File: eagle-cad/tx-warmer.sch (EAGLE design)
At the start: 22 parts

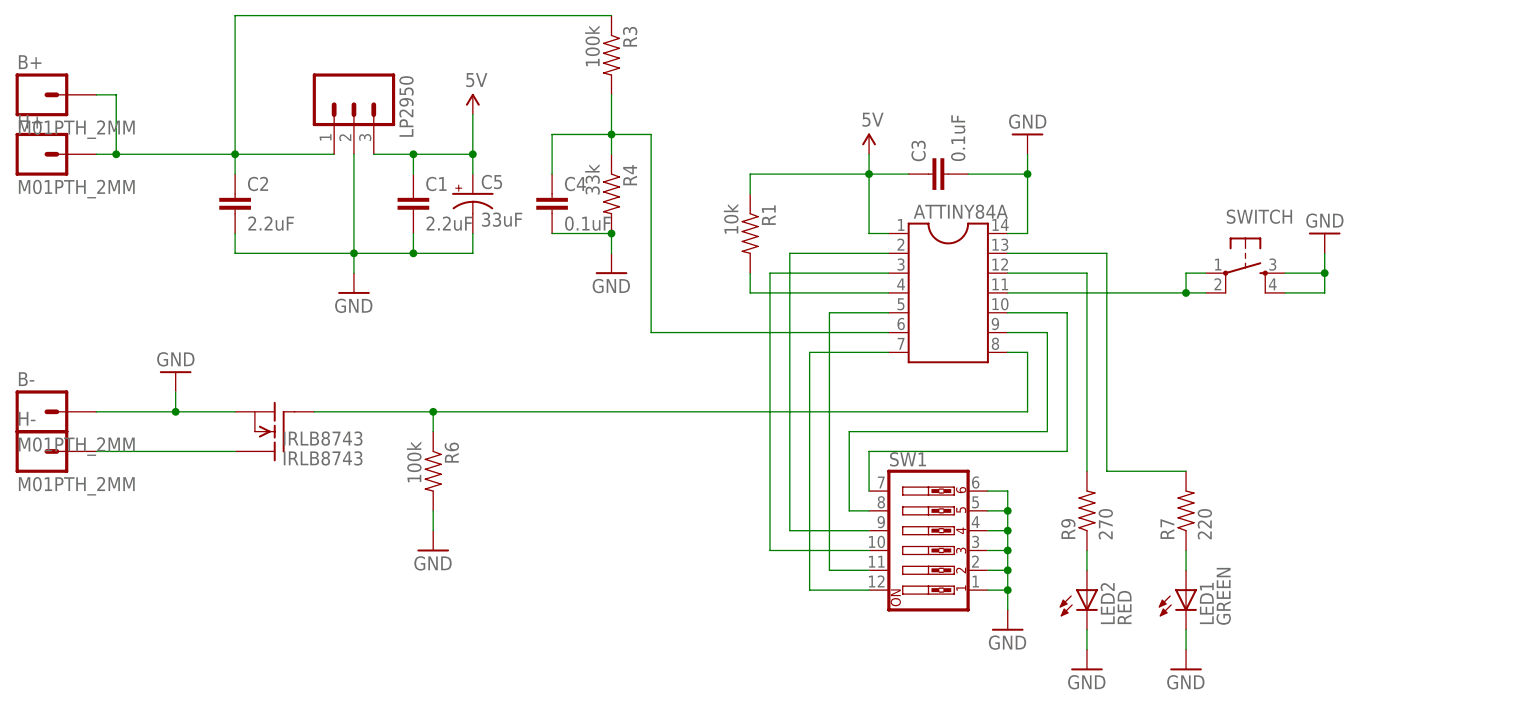
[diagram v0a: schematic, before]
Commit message: Removed DIP:s, added two sensor ports, bat-pins and prog-interface
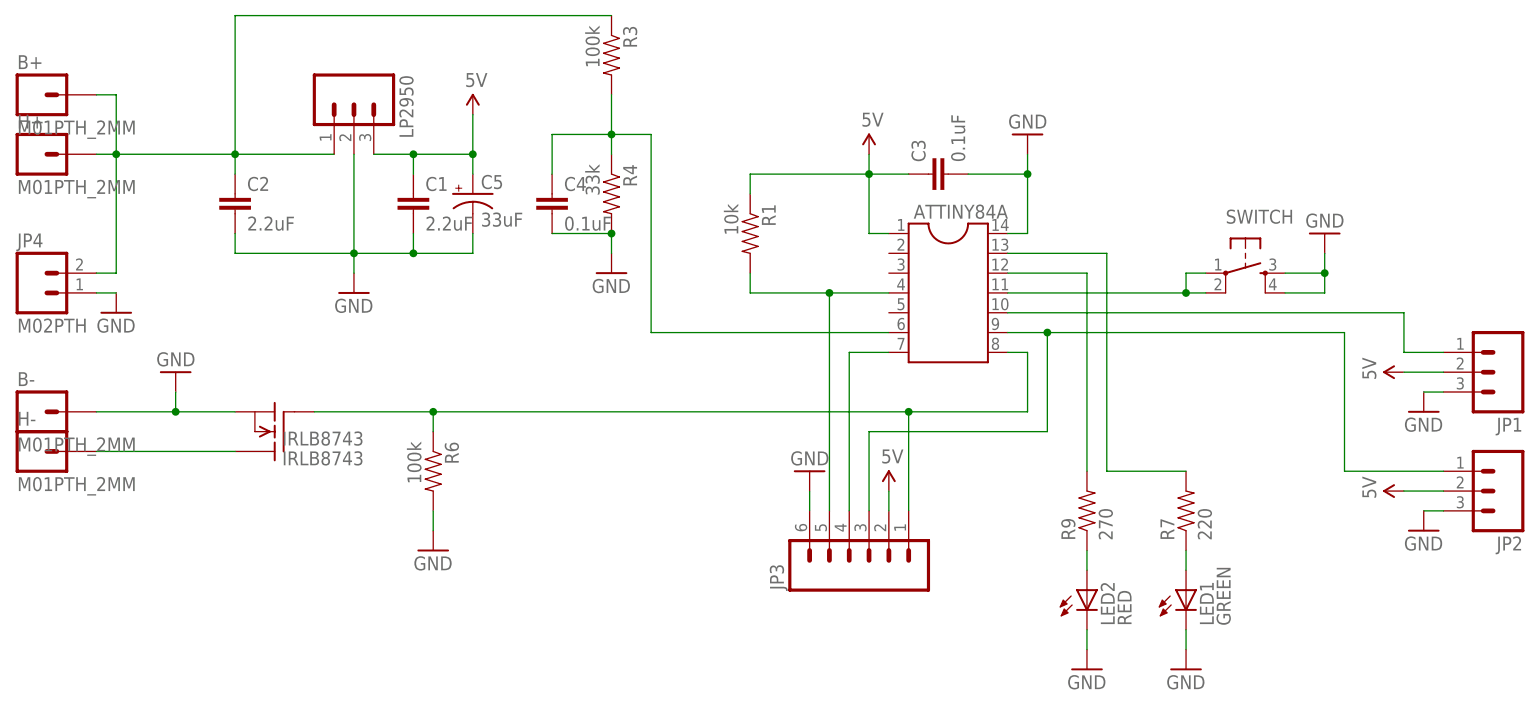
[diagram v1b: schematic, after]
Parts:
- removed SW1: (no value), special:SW_DIP-6
- added JP1, JP2: (no value), SparkFun-Connectors:M03PTH
- added JP3: (no value), SparkFun-Connectors:M06SIP
- added JP4: M02PTH, SparkFun-Connectors:M02PTH
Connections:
- removed net N$20: ATTINY84A.10, SW1.7
- removed net N$21: ATTINY84A.3, SW1.10
- removed net N$5: ATTINY84A.9, SW1.8
- net 5V: now also JP1.2, JP2.2, JP3.2
- net GND: now also JP1.3, JP2.3, JP3.6, JP4.1; no longer SW1.1, SW1.2, SW1.3, SW1.4, SW1.5, SW1.6
- net N$1: now also ATTINY84A.9, JP2.1, JP3.3; no longer ATTINY84A.7, SW1.12
- net N$11: now also JP3.5
- net N$2: now also ATTINY84A.7, JP3.4; no longer ATTINY84A.5, SW1.11
- net N$3: now also ATTINY84A.10, JP1.1; no longer ATTINY84A.2, SW1.9
- net N$4: now also JP4.2
- net N$6: now also JP3.1

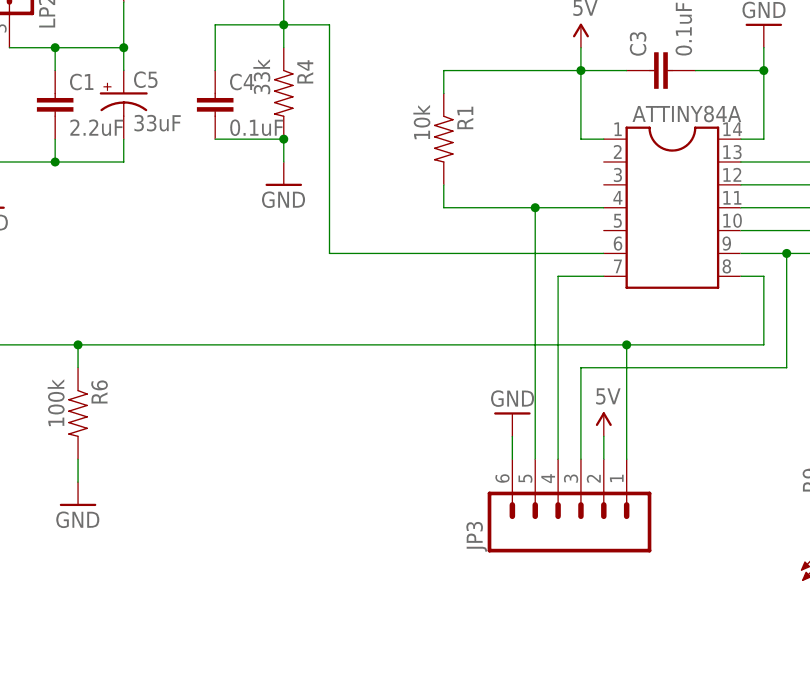
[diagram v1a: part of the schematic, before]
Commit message: Added SMD-jumpers to empty MC-pins
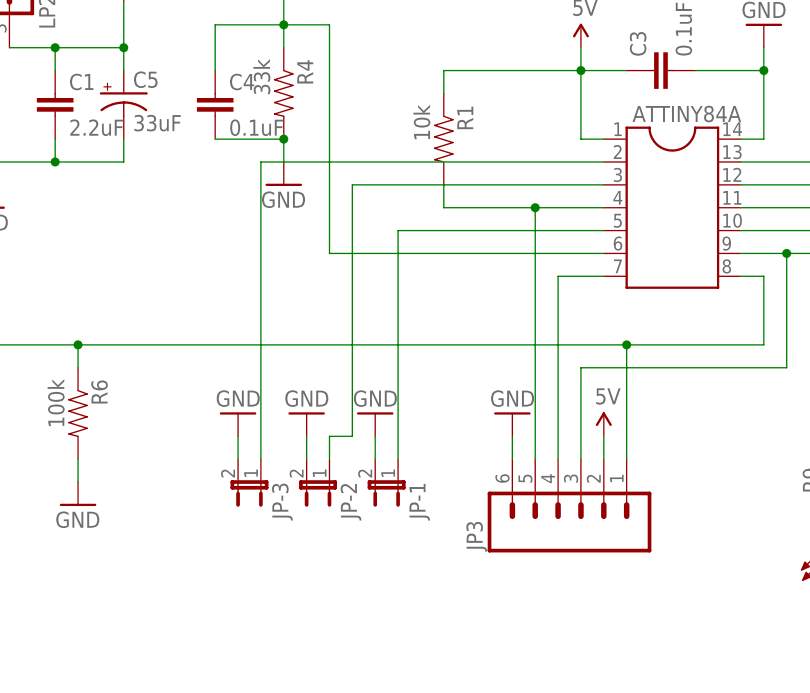
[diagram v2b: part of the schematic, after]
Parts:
- added JP-1, JP-2, JP-3: (no value), SparkFun-Passives:JUMPER-2SMD-NO
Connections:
- new net N$20: ATTINY84A.3, JP-2.1
- new net N$21: ATTINY84A.2, JP-3.1
- new net N$5: ATTINY84A.5, JP-1.1
- net GND: now also JP-1.2, JP-2.2, JP-3.2
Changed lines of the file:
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@@
 <part name="JP4" library="SparkFun-Connectors" deviceset="M02" device="PTH"/>
 <part name="GND12" library="SparkFun-Aesthetics" deviceset="GND" device=""/>
+<part name="JP-1" library="SparkFun-Passives" deviceset="JUMPER-2" device="SMD-NO"/>
+<part name="JP-2" library="SparkFun-Passives" deviceset="JUMPER-2" device="SMD-NO"/>
+<part name="JP-3" library="SparkFun-Passives" deviceset="JUMPER-2" device="SMD-NO"/>
+<part name="GND13" library="SparkFun-Aesthetics" deviceset="GND" device=""/>
+<part name="GND14" library="SparkFun-Aesthetics" deviceset="GND" device=""/>
+<part name="GND15" library="SparkFun-Aesthetics" deviceset="GND" device=""/>
 </parts>
 <sheets>
@@
 <instance part="JP4" gate="G$1" x="-5.08" y="53.34"/>
 <instance part="GND12" gate="1" x="5.08" y="50.8"/>
+<instance part="JP-1" gate="A" x="81.28" y="22.86" rot="R180"/>
+<instance part="JP-2" gate="A" x="73.66" y="22.86" rot="R180"/>
+<instance part="JP-3" gate="A" x="66.04" y="22.86" rot="R180"/>
+<instance part="GND13" gate="1" x="78.74" y="30.48" rot="R180"/>
+<instance part="GND14" gate="1" x="71.12" y="30.48" rot="R180"/>
+<instance part="GND15" gate="1" x="63.5" y="30.48" rot="R180"/>
 </instances>
 <busses>
@@
 <wire x1="2.54" y1="53.34" x2="5.08" y2="53.34" width="0.1524" layer="91"/>
 </segment>
+<segment>
+<pinref part="GND15" gate="1" pin="GND"/>
+<pinref part="JP-3" gate="A" pin="2"/>
+<wire x1="63.5" y1="27.94" x2="63.5" y2="25.4" width="0.1524" layer="91"/>
+</segment>
+<segment>
+<pinref part="GND14" gate="1" pin="GND"/>
+<pinref part="JP-2" gate="A" pin="2"/>
+<wire x1="71.12" y1="27.94" x2="71.12" y2="25.4" width="0.1524" layer="91"/>
+</segment>
+<segment>
+<pinref part="GND13" gate="1" pin="GND"/>
+<pinref part="JP-1" gate="A" pin="2"/>
+<wire x1="78.74" y1="27.94" x2="78.74" y2="25.4" width="0.1524" layer="91"/>
+</segment>
 </net>
 <net name="5V" class="0">
@@
 </segment>
 </net>
+<net name="N$5" class="0">
+<segment>
+<pinref part="ATTINY84A" gate="G$1" pin="5"/>
+<pinref part="JP-1" gate="A" pin="1"/>
+<wire x1="104.14" y1="50.8" x2="81.28" y2="50.8" width="0.1524" layer="91"/>
+<wire x1="81.28" y1="50.8" x2="81.28" y2="25.4" width="0.1524" layer="91"/>
+</segment>
+</net>
+<net name="N$20" class="0">
+<segment>
+<pinref part="ATTINY84A" gate="G$1" pin="3"/>
+<wire x1="104.14" y1="55.88" x2="76.2" y2="55.88" width="0.1524" layer="91"/>
+<wire x1="76.2" y1="55.88" x2="76.2" y2="27.94" width="0.1524" layer="91"/>
+<pinref part="JP-2" gate="A" pin="1"/>
+<wire x1="76.2" y1="27.94" x2="73.66" y2="27.94" width="0.1524" layer="91"/>
+<wire x1="73.66" y1="27.94" x2="73.66" y2="25.4" width="0.1524" layer="91"/>
+</segment>
+</net>
+<net name="N$21" class="0">
+<segment>
+<pinref part="ATTINY84A" gate="G$1" pin="2"/>
+<pinref part="JP-3" gate="A" pin="1"/>
+<wire x1="104.14" y1="58.42" x2="66.04" y2="58.42" width="0.1524" layer="91"/>
+<wire x1="66.04" y1="58.42" x2="66.04" y2="25.4" width="0.1524" layer="91"/>
+</segment>
+</net>
